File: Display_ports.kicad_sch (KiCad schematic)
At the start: 9 parts, among them J2 DP_A

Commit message: More DP
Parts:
- added C41, C42, C43, C44, C45, C46, C47, C48, C49, C50, C51, C52, C53, C54, C55, C56: 0.1uF, Capacitor_SMD:C_0402_1005Metric, symbol Device:C_Small
- added J3: DP_B, A-my-stuff:DP-SMD_HYC16-DP20-178, symbol A-my-stuff:HYC16-DP20-178
- added J4: DP_C, A-my-stuff:DP-SMD_HYC16-DP20-178, symbol A-my-stuff:HYC16-DP20-178
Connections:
- new net: J3.11 (GND), J3.2 (GND), J3.21 (GND), J3.22 (GND), J3.23 (GND), J3.24 (GND), J3.5 (GND), J3.8 (GND)
- new net: J4.11 (GND), J4.2 (GND), J4.21 (GND), J4.22 (GND), J4.23 (GND), J4.24 (GND), J4.5 (GND), J4.8 (GND)
- new net iGPU_DDI2_C_TX0+: C41.2, J3.1 (ML_LANE0_P)
- new net iGPU_DDI2_C_TX0-: C42.2, J3.3 (ML_LANE0_N)
- new net iGPU_DDI2_C_TX1+: C43.2, J3.4 (ML_LANE1_P)
- new net iGPU_DDI2_C_TX1-: C44.2, J3.6 (ML_LANE1_N)
- new net iGPU_DDI2_C_TX2+: C45.2, J3.7 (ML_LANE2_P)
- new net iGPU_DDI2_C_TX2-: C46.2, J3.9 (ML_LANE2_N)
- new net iGPU_DDI2_C_TX3+: C47.2, J3.10 (ML_LANE3_P)
- new net iGPU_DDI2_C_TX3-: C48.2, J3.12 (ML_LANE3_N)
- new net iGPU_DDI2_TX0+: C41.1
- new net iGPU_DDI2_TX0-: C42.1
- new net iGPU_DDI2_TX1+: C43.1
- new net iGPU_DDI2_TX1-: C44.1
- new net iGPU_DDI2_TX2+: C45.1
- new net iGPU_DDI2_TX2-: C46.1
- new net iGPU_DDI2_TX3+: C47.1
- new net iGPU_DDI2_TX3-: C48.1
- new net iGPU_DDI3_C_TX0+: C49.2, J4.1 (ML_LANE0_P)
- new net iGPU_DDI3_C_TX0-: C50.2, J4.3 (ML_LANE0_N)
- new net iGPU_DDI3_C_TX1+: C51.2, J4.4 (ML_LANE1_P)
- new net iGPU_DDI3_C_TX1-: C52.2, J4.6 (ML_LANE1_N)
- new net iGPU_DDI3_C_TX2+: C53.2, J4.7 (ML_LANE2_P)
- new net iGPU_DDI3_C_TX2-: C54.2, J4.9 (ML_LANE2_N)
- new net iGPU_DDI3_C_TX3+: C55.2, J4.10 (ML_LANE3_P)
- new net iGPU_DDI3_C_TX3-: C56.2, J4.12 (ML_LANE3_N)
- new net iGPU_DDI3_TX0+: C49.1
- new net iGPU_DDI3_TX0-: C50.1
- new net iGPU_DDI3_TX1+: C51.1
- new net iGPU_DDI3_TX1-: C52.1
- new net iGPU_DDI3_TX2+: C53.1
- new net iGPU_DDI3_TX2-: C54.1
- new net iGPU_DDI3_TX3+: C55.1
- new net iGPU_DDI3_TX3-: C56.1

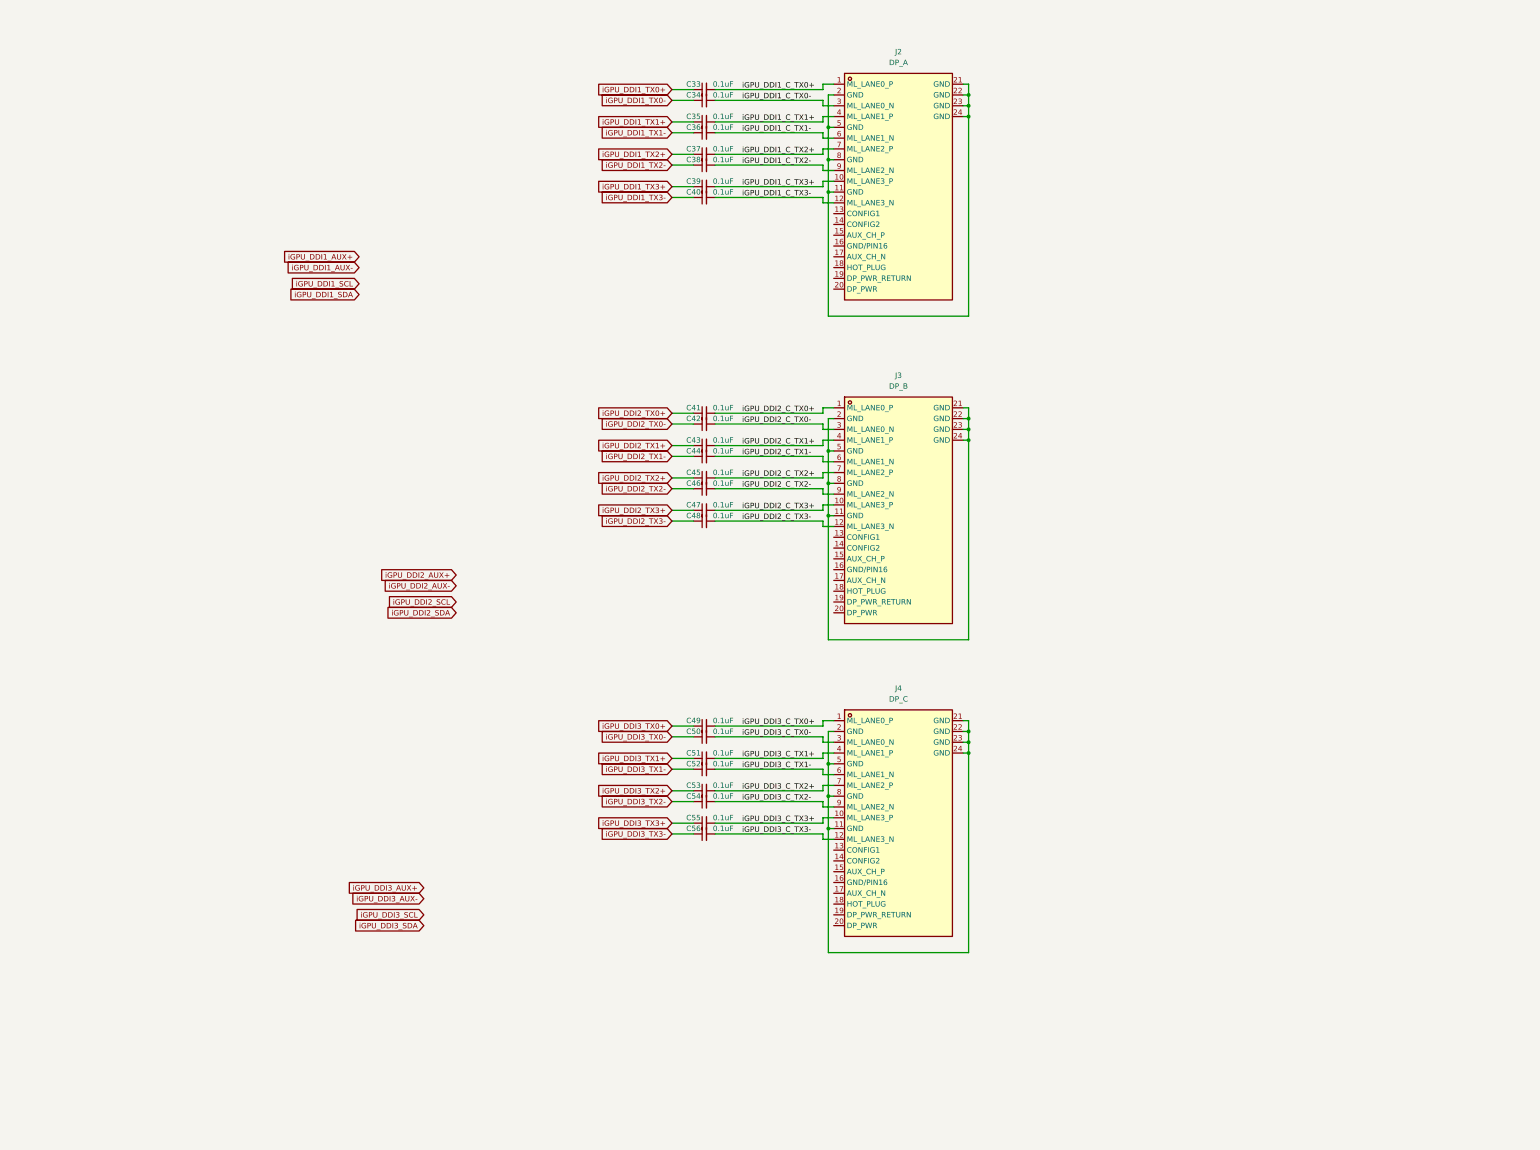
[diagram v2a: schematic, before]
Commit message: Added DP_A DP++ HDMI dongle detection circuit
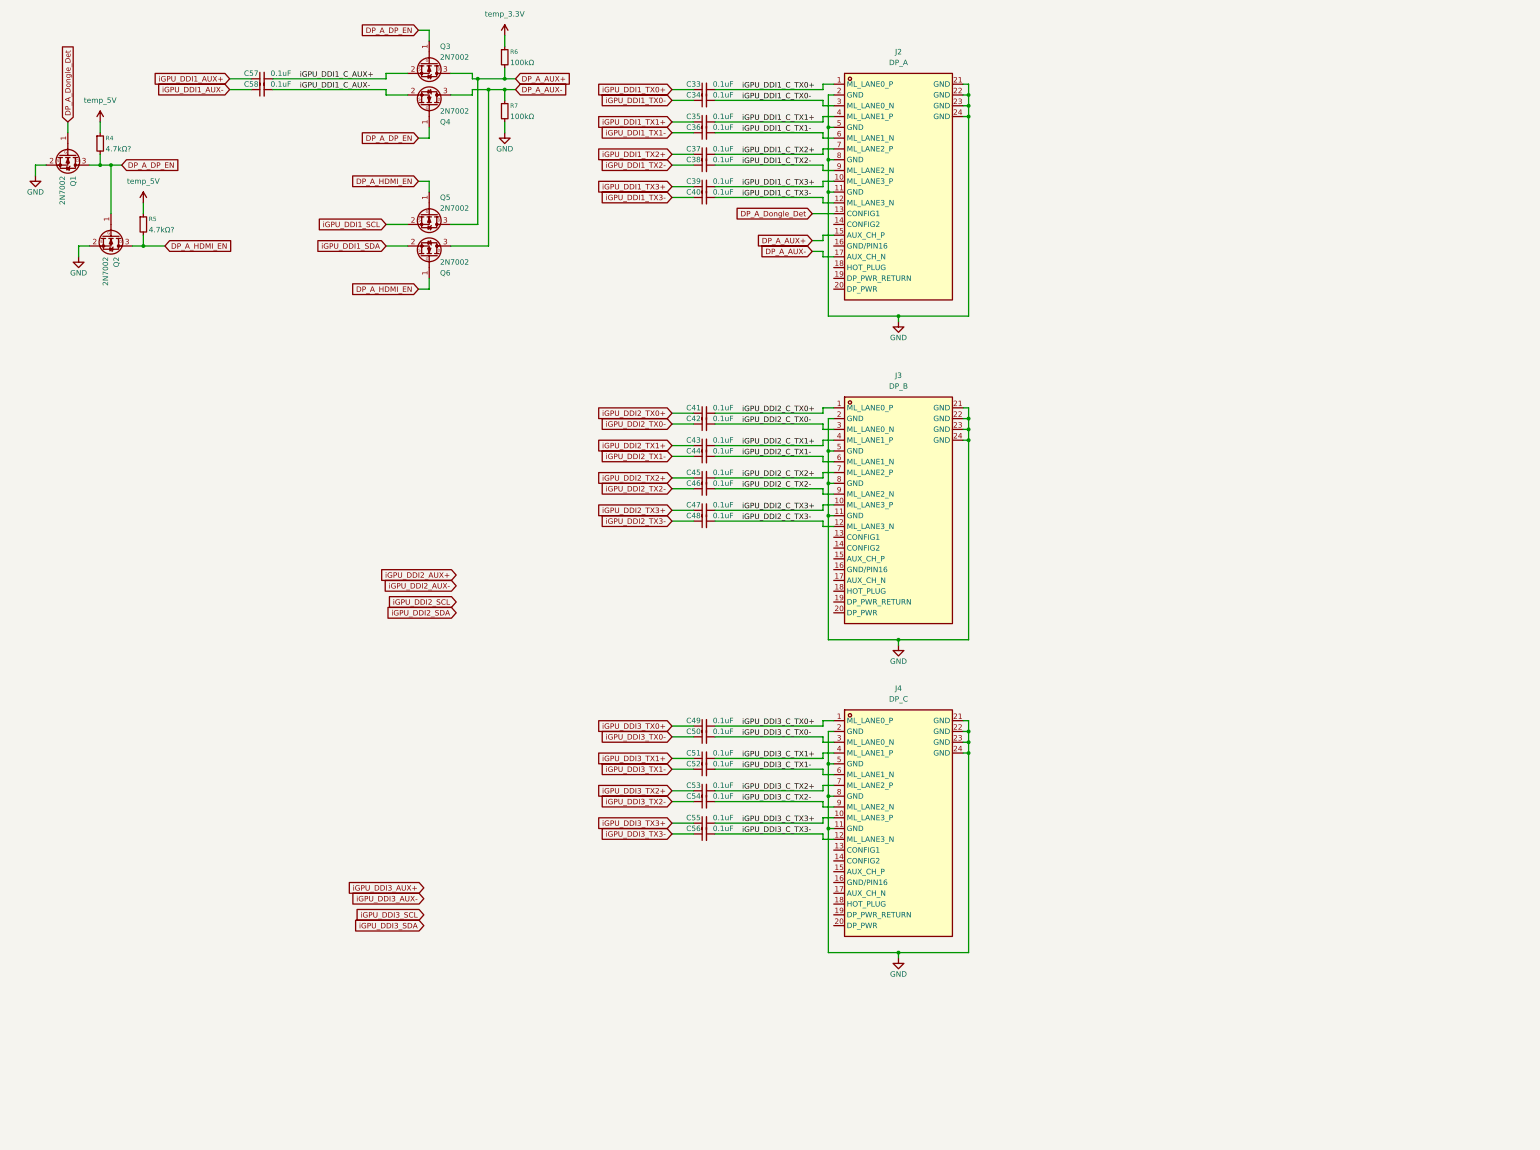
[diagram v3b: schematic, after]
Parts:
- added C57, C58: 0.1uF, Capacitor_SMD:C_0402_1005Metric, symbol Device:C_Small
- added Q1, Q2, Q3, Q4, Q5, Q6: 2N7002, Package_TO_SOT_SMD:SOT-23, symbol Transistor_FET:2N7002
- added R4, R5: 4.7kΩ?, Resistor_SMD:R_0402_1005Metric, symbol Device:R_Small
- added R6, R7: 100kΩ, Resistor_SMD:R_0402_1005Metric, symbol Device:R_Small
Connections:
- net iGPU_DDI1_AUX+: now also C57.1
- net iGPU_DDI1_AUX-: now also C58.1
- net iGPU_DDI1_SCL: now also Q5.2 (S)
- net iGPU_DDI1_SDA: now also Q6.2 (S)
- net GND: now reaches J3.11 (GND), J3.2 (GND), J3.21 (GND), J3.22 (GND), J3.23 (GND), J3.24 (GND), J3.5 (GND), J3.8 (GND)
- net GND: now also J2.11 (GND), J2.2 (GND), J2.21 (GND), J2.22 (GND), J2.23 (GND), J2.24 (GND), J2.5 (GND), J2.8 (GND), J4.11 (GND), J4.2 (GND), J4.21 (GND), J4.22 (GND), J4.23 (GND), J4.24 (GND), J4.5 (GND), J4.8 (GND), Q1.2 (S), Q2.2 (S), R7.2
- net DP_A_Dongle_Det: now reaches J2.13 (CONFIG1)
- net DP_A_Dongle_Det: now also Q1.1 (G)
- net DP_A_AUX+: now reaches J2.15 (AUX_CH_P)
- net DP_A_AUX+: now also Q3.3 (D), Q5.3 (D), R6.2
- net DP_A_AUX-: now reaches J2.17 (AUX_CH_N)
- net DP_A_AUX-: now also Q4.3 (D), Q6.3 (D), R7.1
- new net DP_A_DP_EN: Q1.3 (D), Q2.1 (G), Q3.1 (G), Q4.1 (G), R4.2
- new net DP_A_HDMI_EN: Q2.3 (D), Q5.1 (G), Q6.1 (G), R5.2
- new net iGPU_DDI1_C_AUX+: C57.2, Q3.2 (S)
- new net iGPU_DDI1_C_AUX-: C58.2, Q4.2 (S)
- new net temp_3.3V: R6.1
- new net temp_5V: R4.1, R5.1

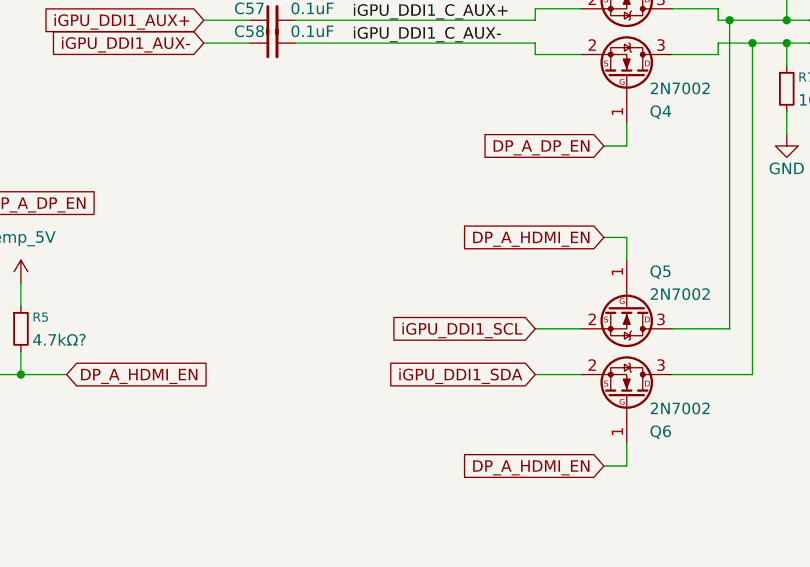
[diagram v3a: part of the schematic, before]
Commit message: added DP_A DDC pullups
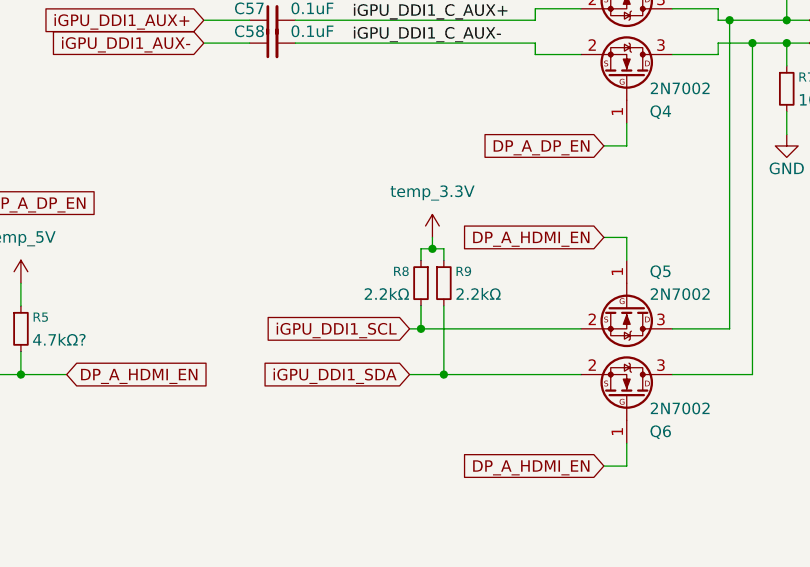
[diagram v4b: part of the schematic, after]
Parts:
- added R8, R9: 2.2kΩ, Resistor_SMD:R_0402_1005Metric, symbol Device:R_Small
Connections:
- net iGPU_DDI1_SCL: now also R8.2
- net iGPU_DDI1_SDA: now also R9.2
- net temp_3.3V: now also R8.1, R9.1

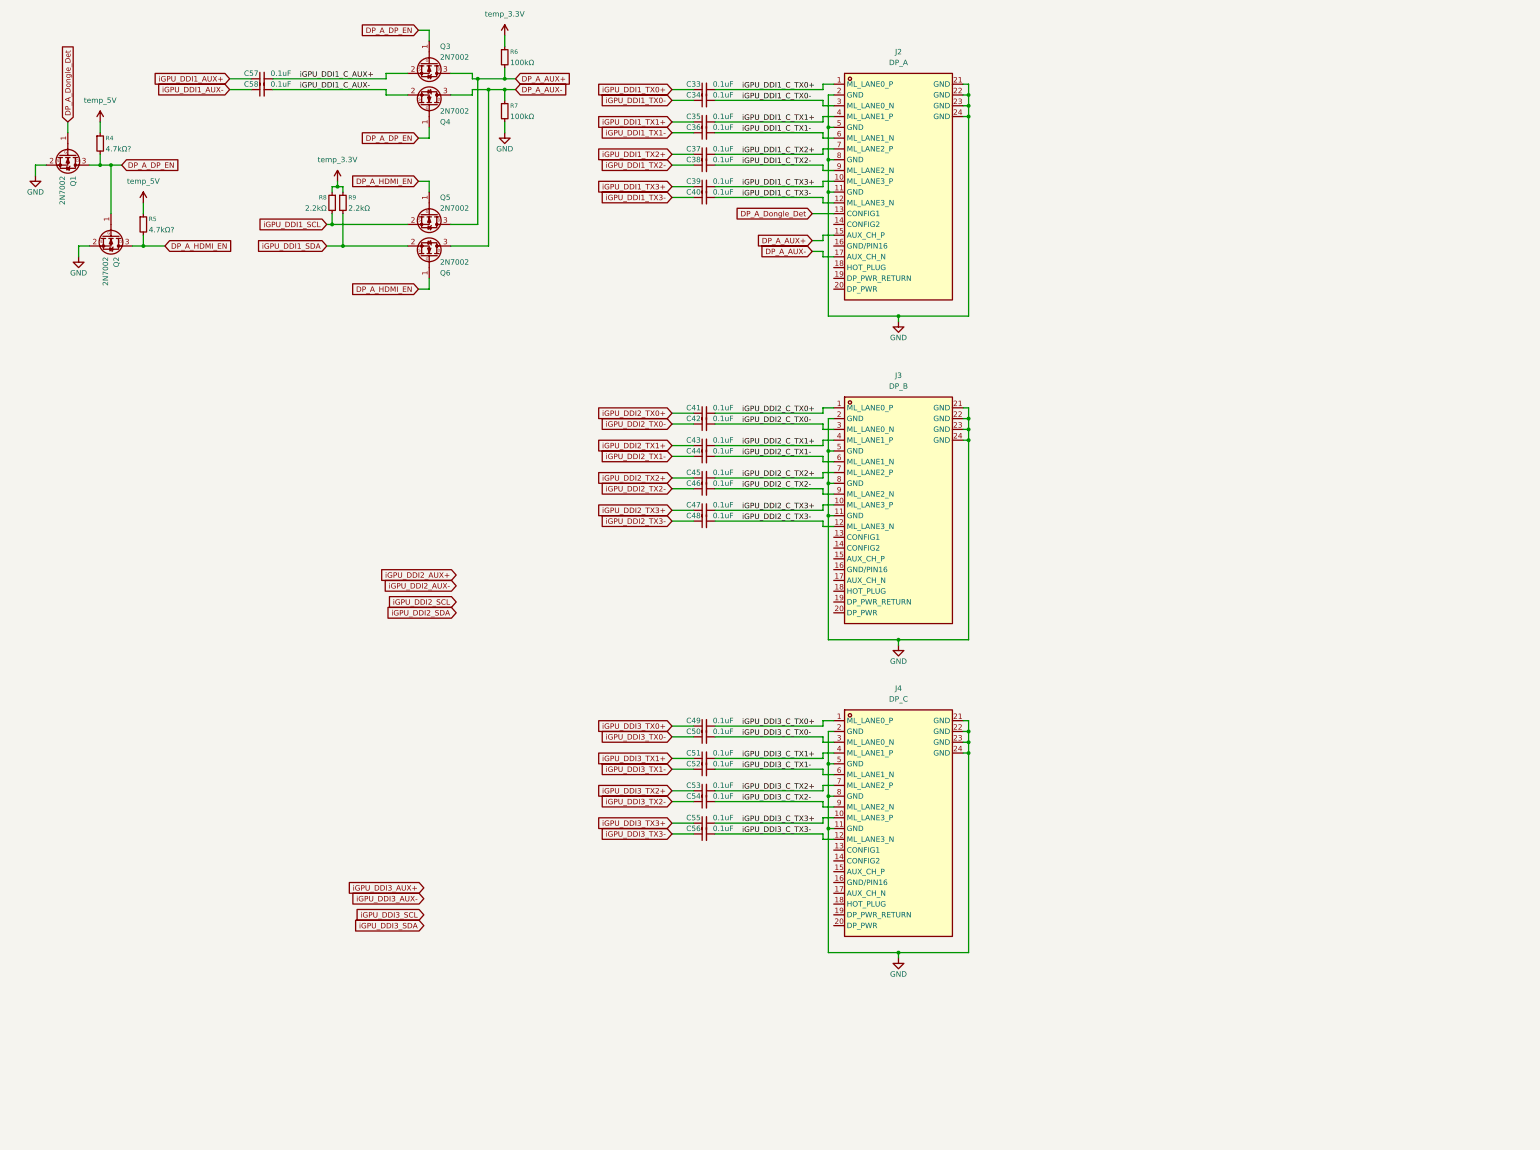
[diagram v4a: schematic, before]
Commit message: partially added eDP + rearranged other display stuff
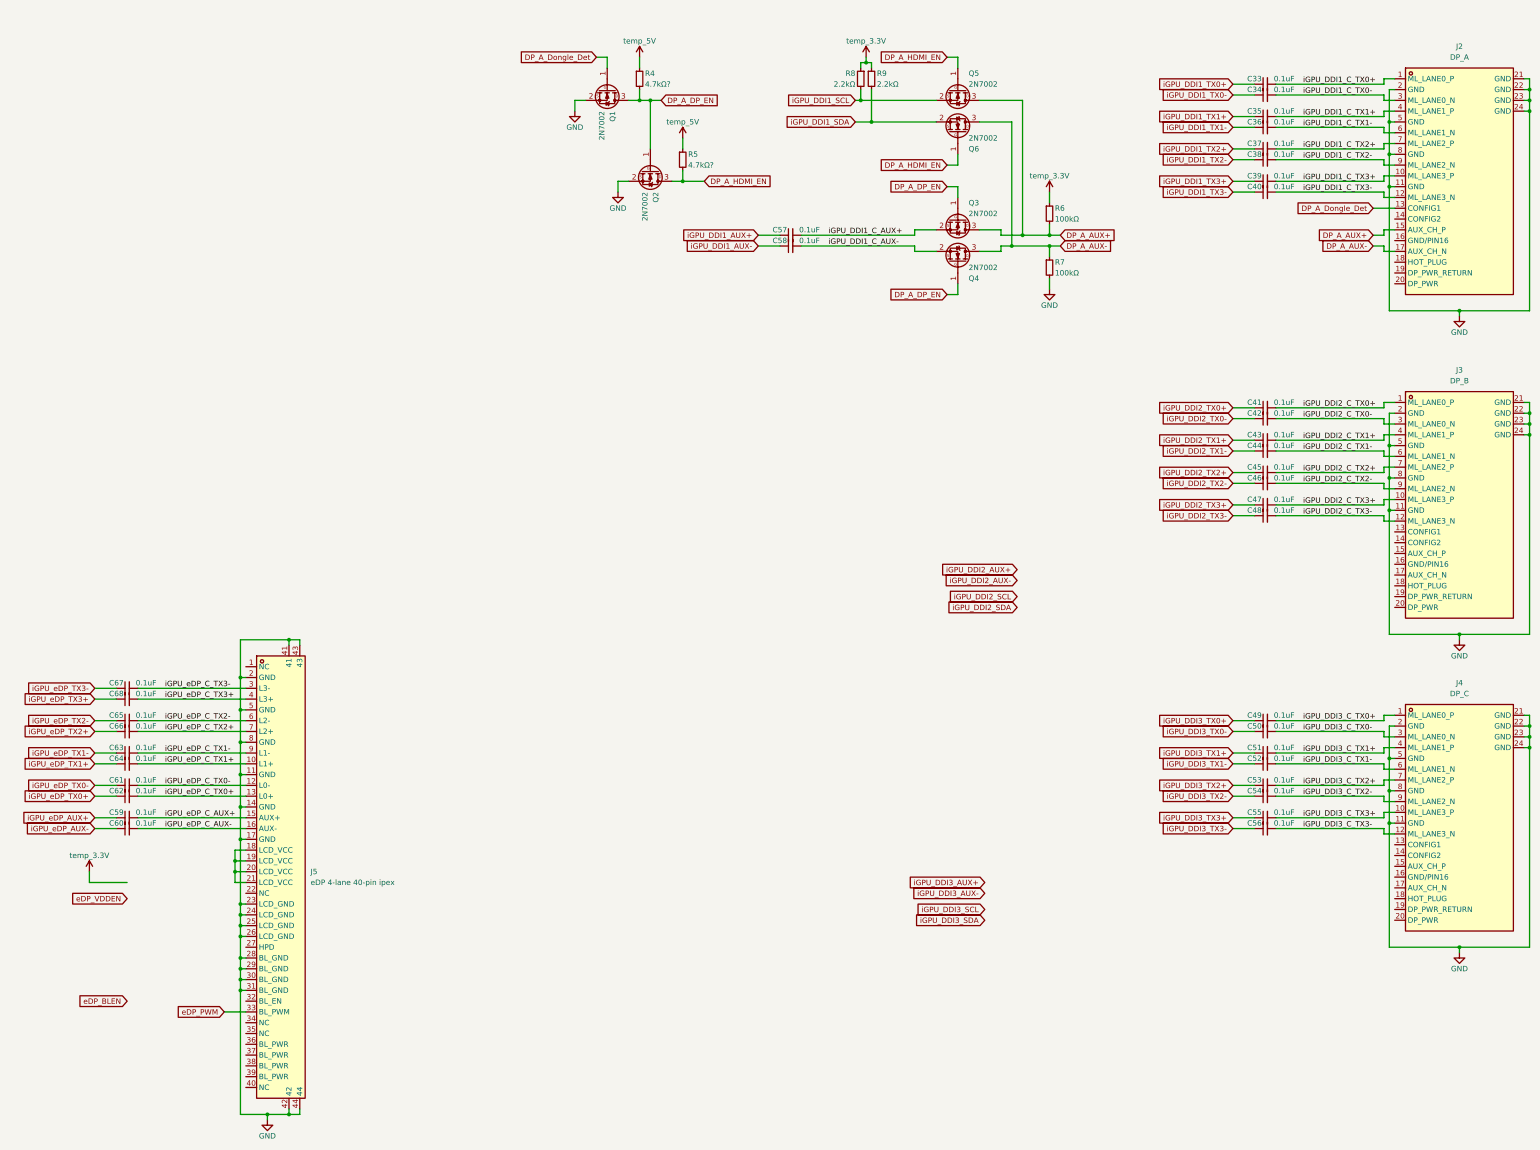
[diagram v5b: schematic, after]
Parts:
- added C59, C60, C61, C62, C63, C64, C65, C66, C67, C68: 0.1uF, Capacitor_SMD:C_0402_1005Metric, symbol Device:C_Small
- added J5: eDP 4-lane 40-pin ipex, symbol A-my-stuff:eDP-4lane-40p-ipex
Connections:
- net GND: now also J5.11 (GND), J5.14 (GND), J5.17 (GND), J5.2 (GND), J5.23 (LCD_GND), J5.24 (LCD_GND), J5.25 (LCD_GND), J5.26 (LCD_GND), J5.28 (BL_GND), J5.29 (BL_GND), J5.30 (BL_GND), J5.31 (BL_GND), J5.41, J5.42, J5.43, J5.44, J5.5 (GND), J5.8 (GND)
- new net: J5.18 (LCD_VCC), J5.19 (LCD_VCC), J5.20 (LCD_VCC), J5.21 (LCD_VCC)
- new net eDP_PWM: J5.33 (BL_PWM)
- new net iGPU_eDP_AUX+: C59.1
- new net iGPU_eDP_AUX-: C60.1
- new net iGPU_eDP_C_AUX+: C59.2, J5.15 (AUX+)
- new net iGPU_eDP_C_AUX-: C60.2, J5.16 (AUX-)
- new net iGPU_eDP_C_TX0+: C62.2, J5.13 (L0+)
- new net iGPU_eDP_C_TX0-: C61.2, J5.12 (L0-)
- new net iGPU_eDP_C_TX1+: C64.2, J5.10 (L1+)
- new net iGPU_eDP_C_TX1-: C63.2, J5.9 (L1-)
- new net iGPU_eDP_C_TX2+: C66.2, J5.7 (L2+)
- new net iGPU_eDP_C_TX2-: C65.2, J5.6 (L2-)
- new net iGPU_eDP_C_TX3+: C68.2, J5.4 (L3+)
- new net iGPU_eDP_C_TX3-: C67.2, J5.3 (L3-)
- new net iGPU_eDP_TX0+: C62.1
- new net iGPU_eDP_TX0-: C61.1
- new net iGPU_eDP_TX1+: C64.1
- new net iGPU_eDP_TX1-: C63.1
- new net iGPU_eDP_TX2+: C66.1
- new net iGPU_eDP_TX2-: C65.1
- new net iGPU_eDP_TX3+: C68.1
- new net iGPU_eDP_TX3-: C67.1
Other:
- moved on the sheet: C33, C34, C35, C36, C37, C38, C39, C40, C41, C42, C43, C44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
